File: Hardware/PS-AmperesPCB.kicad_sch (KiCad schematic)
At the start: 10 parts, among them J1 PeripheralCAN, J2 PeripheralCAN

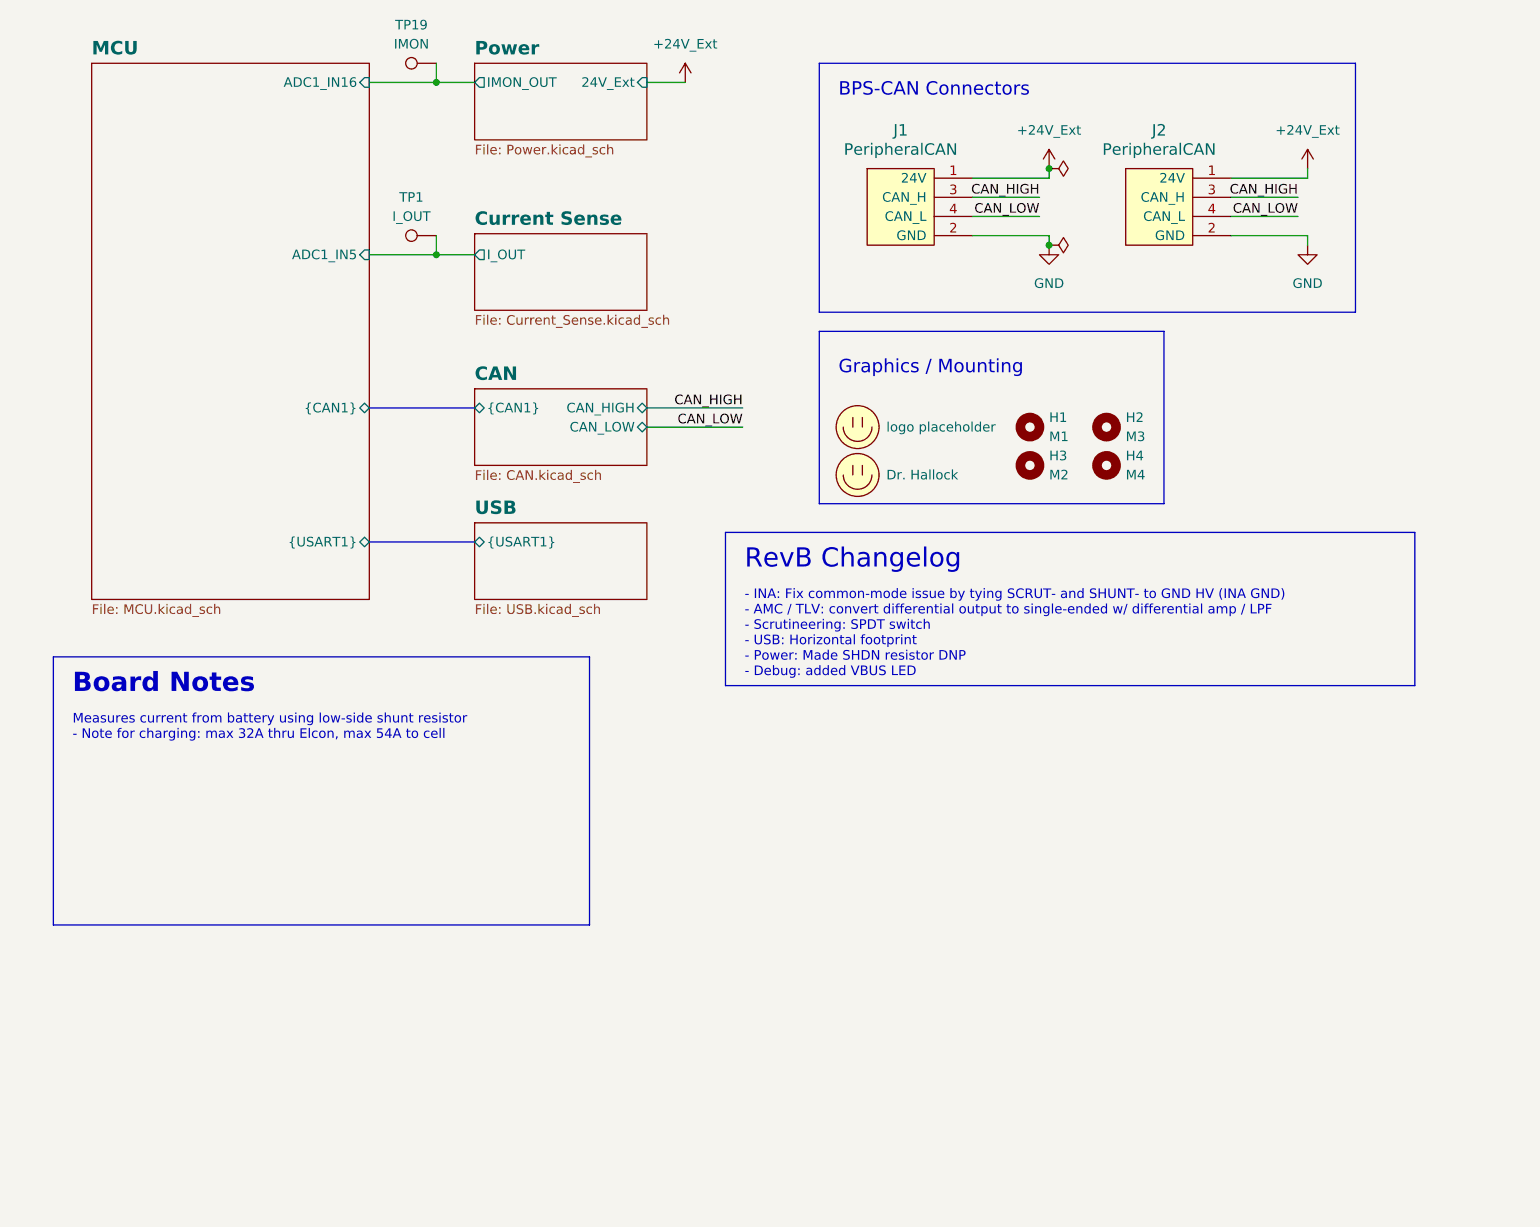
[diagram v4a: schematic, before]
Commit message: refactored and added LPF docs; added fuse, boot_gpio from USB-UART chip
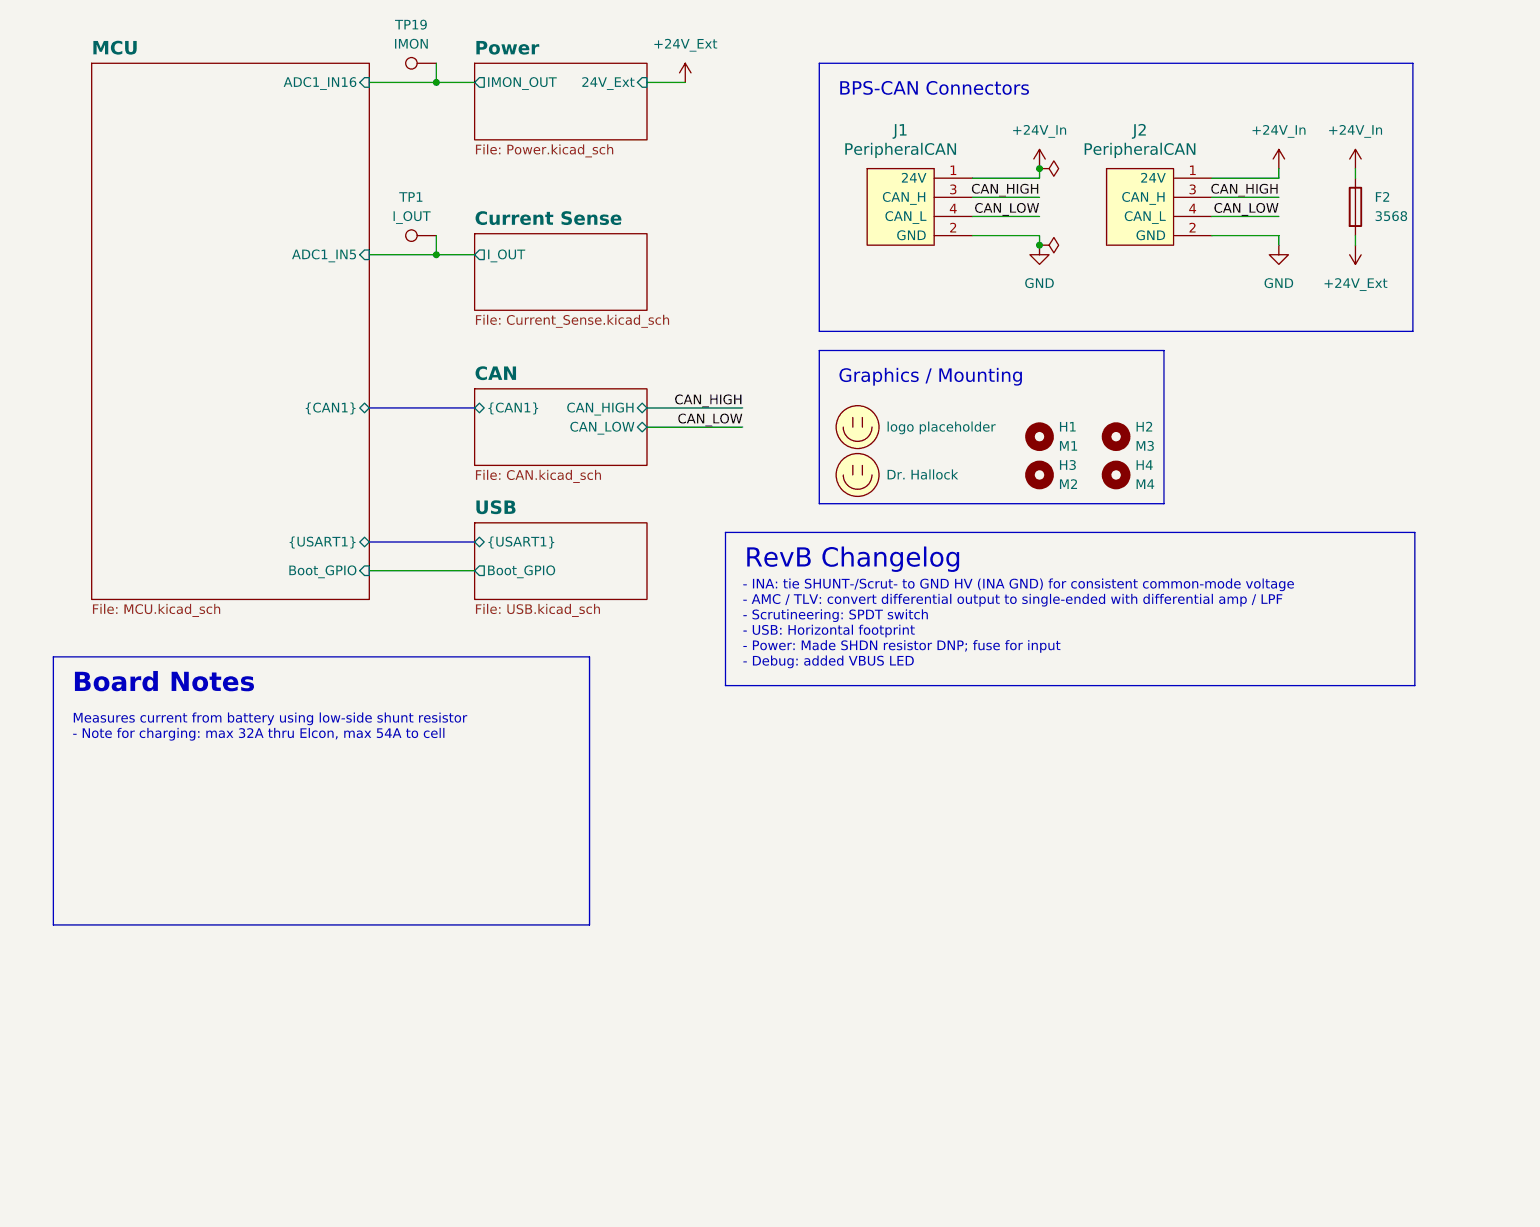
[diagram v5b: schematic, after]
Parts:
- added F2: 3568, Fuse:Fuseholder_Blade_Mini_Keystone_3568, symbol Device:Fuse
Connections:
- net +24V_Ext: now also F2.2; no longer J1.1 (24V), J2.1 (24V)
- new net +24V_In: F2.1, J1.1 (24V), J2.1 (24V)
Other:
- sheet MCU ports: added Boot_GPIO; removed none
- sheet USB ports: added Boot_GPIO; removed none
- note added: "- INA: tie SHUNT-/Scrut- to GND HV (INA GND) for consistent common-mode voltage - AMC / TLV: convert differential output to single-ended with differential amp / LPF - Scrutineering: SPDT switch - USB: Horizontal footprint - Power: Made SHDN resistor DNP; fuse for input - Debug: added VBUS LED"
- note removed: "- INA: Fix common-mode issue by tying SCRUT- and SHUNT- to GND HV (INA GND) - AMC / TLV: convert differential output to single-ended w/ differential amp / LPF - Scrutineering: SPDT switch - USB: Horizontal footprint - Power: Made SHDN resistor DNP - Debug: added VBUS LED"
- moved on the sheet: H1, H2, H3, H4, J2

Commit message: slightly cooked
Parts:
- TP19: footprint TestPoint:TestPoint_Keystone_5005-5009_Compact -> TestPoint:TestPoint_Pad_1.0x1.0mm
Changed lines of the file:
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@@
 			)
 		)
-		(property "Footprint" "TestPoint:TestPoint_Keystone_5005-5009_Compact"
+		(property "Footprint" "TestPoint:TestPoint_Pad_1.0x1.0mm"
 			(at 66.04 15.24 0)
 			(effects

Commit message: layout stuff
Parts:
- TP1: footprint TestPoint:TestPoint_Keystone_5005-5009_Compact -> Connector_PinHeader_2.54mm:PinHeader_1x01_P2.54mm_Vertical
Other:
- note added: "I_OUT = (current * shunt * gain) + Vref (V) = (current * 0.025) + 1.25 (V)"
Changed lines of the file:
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@@
 	(paper "A5")
 	(rectangle
-		(start 15.24 99.06)
+		(start 15.24 96.52)
 		(end 86.36 134.62)
 		(stroke
@@
 	(text "Board Notes"
 		(exclude_from_sim no)
-		(at 17.78 104.14 0)
+		(at 17.78 101.6 0)
 		(effects
 			(font
@@
 		)
 	)
+	(text "I_OUT = (current * shunt * gain) + Vref (V) \n	  = (current * 0.025) + 1.25 (V)"
+		(exclude_from_sim no)
+		(at 17.78 107.696 0)
+		(effects
+			(font
+				(size 1.27 1.27)
+				(thickness 0.254)
+				(bold yes)
+			)
+			(justify left top)
+		)
+	)
 	(text "Graphics / Mounting"
 		(exclude_from_sim no)
@@
 	(text "Measures current from battery using low-side shunt resistor\n- Note for charging: max 32A thru Elcon, max 54A to cell\n"
 		(exclude_from_sim no)
-		(at 17.78 106.68 0)
+		(at 17.78 102.616 0)
 		(effects
 			(font
@@
 			(table_cell "Measurable Current Range"
 				(exclude_from_sim no)
-				(at 17.78 122.936 0)
+				(at 17.78 123.444 0)
 				(size 27.94 3.048)
 				(margins 0.9525 0.9525 0.9525 0.9525)
@@
 			(table_cell "Current (A)"
 				(exclude_from_sim no)
-				(at 45.72 122.936 0)
+				(at 45.72 123.444 0)
 				(size 15.24 3.048)
 				(margins 0.9525 0.9525 0.9525 0.9525)
@@
 			(table_cell "I_OUT Reading (V)"
 				(exclude_from_sim no)
-				(at 60.96 122.936 0)
+				(at 60.96 123.444 0)
 				(size 20.32 3.048)
 				(margins 0.9525 0.9525 0.9525 0.9525)
@@
 			(table_cell "Max Charge (-)"
 				(exclude_from_sim no)
-				(at 17.78 125.984 0)
+				(at 17.78 126.492 0)
 				(size 27.94 3.048)
 				(margins 0.9525 0.9525 0.9525 0.9525)
@@
 			(table_cell "-46 A"
 				(exclude_from_sim no)
-				(at 45.72 125.984 0)
+				(at 45.72 126.492 0)
 				(size 15.24 3.048)
 				(margins 0.9525 0.9525 0.9525 0.9525)
@@
 			(table_cell "0.1 V"
 				(exclude_from_sim no)
-				(at 60.96 125.984 0)
+				(at 60.96 126.492 0)
 				(size 20.32 3.048)
 				(margins 0.9525 0.9525 0.9525 0.9525)
@@
 			(table_cell "Max Discharge (+)"
 				(exclude_from_sim no)
-				(at 17.78 129.032 0)
+				(at 17.78 129.54 0)
 				(size 27.94 3.048)
 				(margins 0.9525 0.9525 0.9525 0.9525)
@@
 			(table_cell "+78 A"
 				(exclude_from_sim no)
-				(at 45.72 129.032 0)
+				(at 45.72 129.54 0)
 				(size 15.24 3.048)
 				(margins 0.9525 0.9525 0.9525 0.9525)
@@
 			(table_cell "3.2 V"
 				(exclude_from_sim no)
-				(at 60.96 129.032 0)
+				(at 60.96 129.54 0)
 				(size 20.32 3.048)
 				(margins 0.9525 0.9525 0.9525 0.9525)
@@
 			(table_cell "Battery Current Range"
 				(exclude_from_sim no)
-				(at 17.78 111.76 0)
+				(at 17.78 112.268 0)
 				(size 27.94 3.048)
 				(margins 0.9525 0.9525 0.9525 0.9525)
@@
 			(table_cell "Current (A)"
 				(exclude_from_sim no)
-				(at 45.72 111.76 0)
+				(at 45.72 112.268 0)
 				(size 15.24 3.048)
 				(margins 0.9525 0.9525 0.9525 0.9525)
@@
 			(table_cell "I_OUT Reading (V)"
 				(exclude_from_sim no)
-				(at 60.96 111.76 0)
+				(at 60.96 112.268 0)
 				(size 20.32 3.048)
 				(margins 0.9525 0.9525 0.9525 0.9525)
@@
 			(table_cell "Max Charge (-)"
 				(exclude_from_sim no)
-				(at 17.78 114.808 0)
+				(at 17.78 115.316 0)
 				(size 27.94 3.048)
 				(margins 0.9525 0.9525 0.9525 0.9525)
@@
 			(table_cell "-32 A"
 				(exclude_from_sim no)
-				(at 45.72 114.808 0)
+				(at 45.72 115.316 0)
 				(size 15.24 3.048)
 				(margins 0.9525 0.9525 0.9525 0.9525)
@@
 			(table_cell "0.45 V"
 				(exclude_from_sim no)
-				(at 60.96 114.808 0)
+				(at 60.96 115.316 0)
 				(size 20.32 3.048)
 				(margins 0.9525 0.9525 0.9525 0.9525)
@@
 			(table_cell "Max Discharge (+)"
 				(exclude_from_sim no)
-				(at 17.78 117.856 0)
+				(at 17.78 118.364 0)
 				(size 27.94 3.048)
 				(margins 0.9525 0.9525 0.9525 0.9525)
@@
 			(table_cell "+70 A"
 				(exclude_from_sim no)
-				(at 45.72 117.856 0)
+				(at 45.72 118.364 0)
 				(size 15.24 3.048)
 				(margins 0.9525 0.9525 0.9525 0.9525)
@@
 			(table_cell "3.0 V"
 				(exclude_from_sim no)
-				(at 60.96 117.856 0)
+				(at 60.96 118.364 0)
 				(size 20.32 3.048)
 				(margins 0.9525 0.9525 0.9525 0.9525)
@@
 			)
 		)
-		(property "Footprint" "TestPoint:TestPoint_Keystone_5005-5009_Compact"
+		(property "Footprint" "Connector_PinHeader_2.54mm:PinHeader_1x01_P2.54mm_Vertical"
 			(at 66.04 38.1 0)
 			(effects

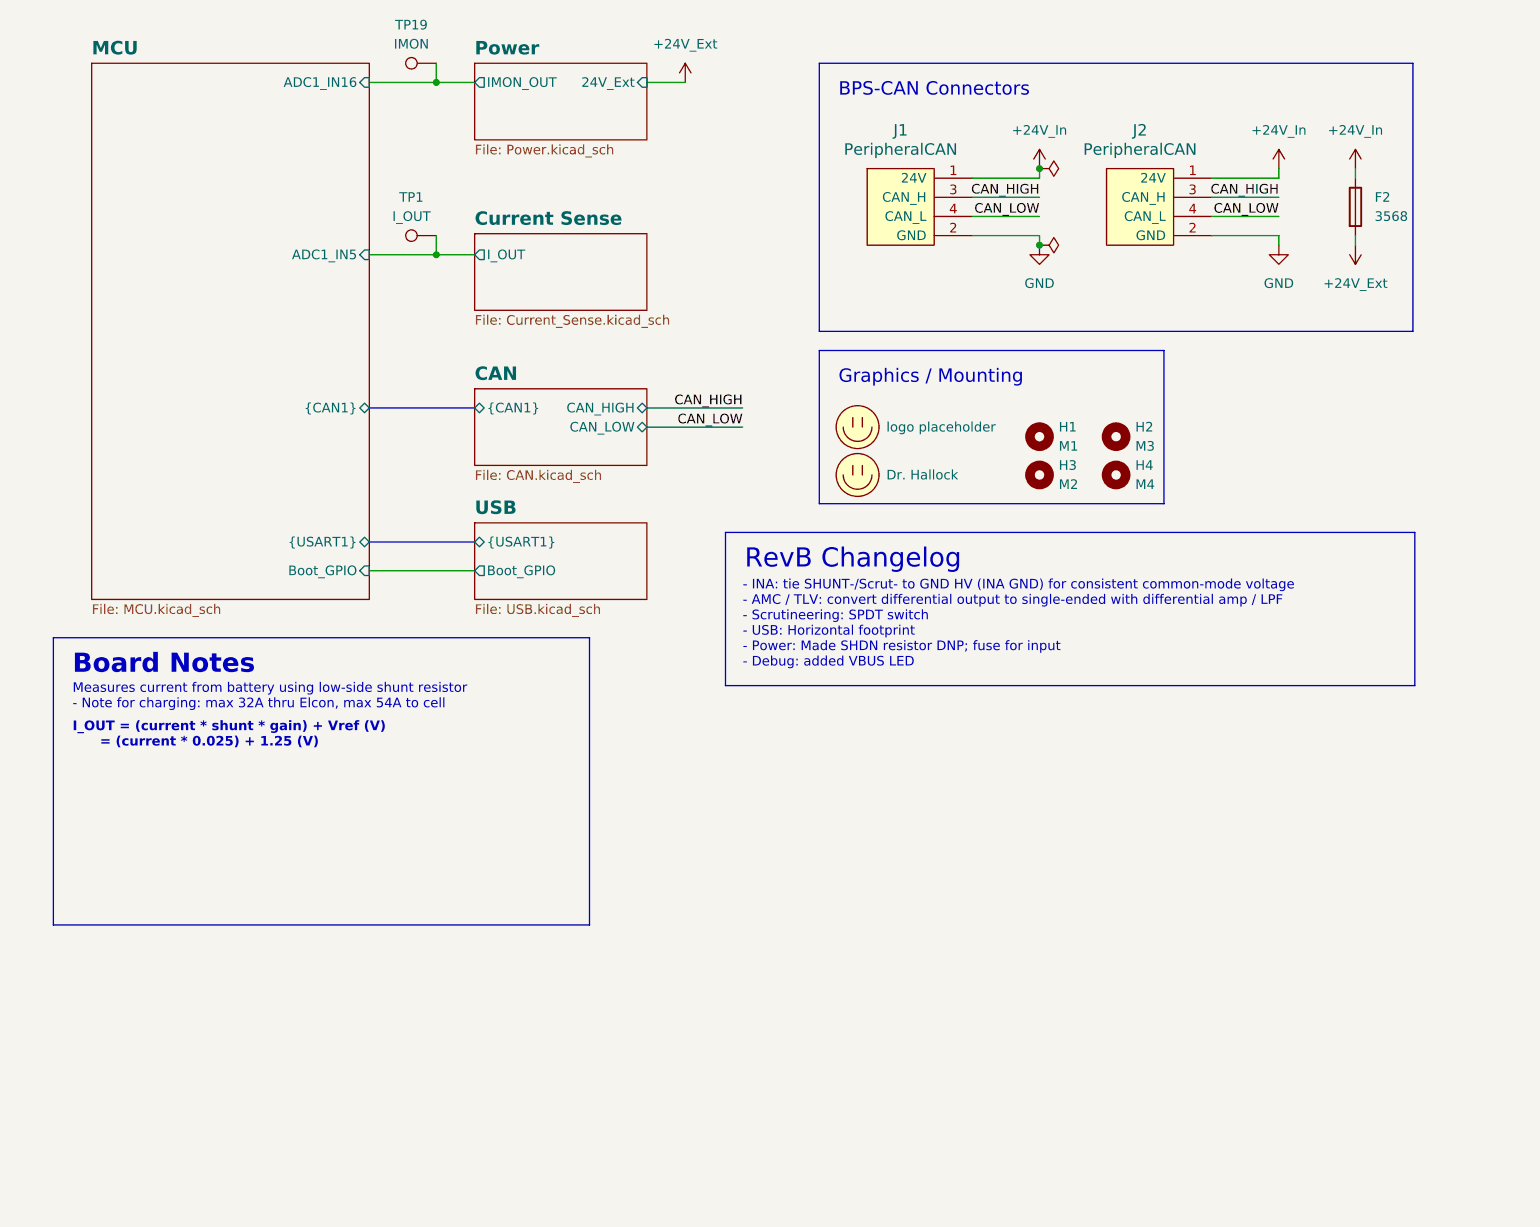
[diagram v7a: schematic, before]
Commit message: post review council sch changes: shielded connectors, removed SHDN resistor, diode OR for boot, standardized resistors
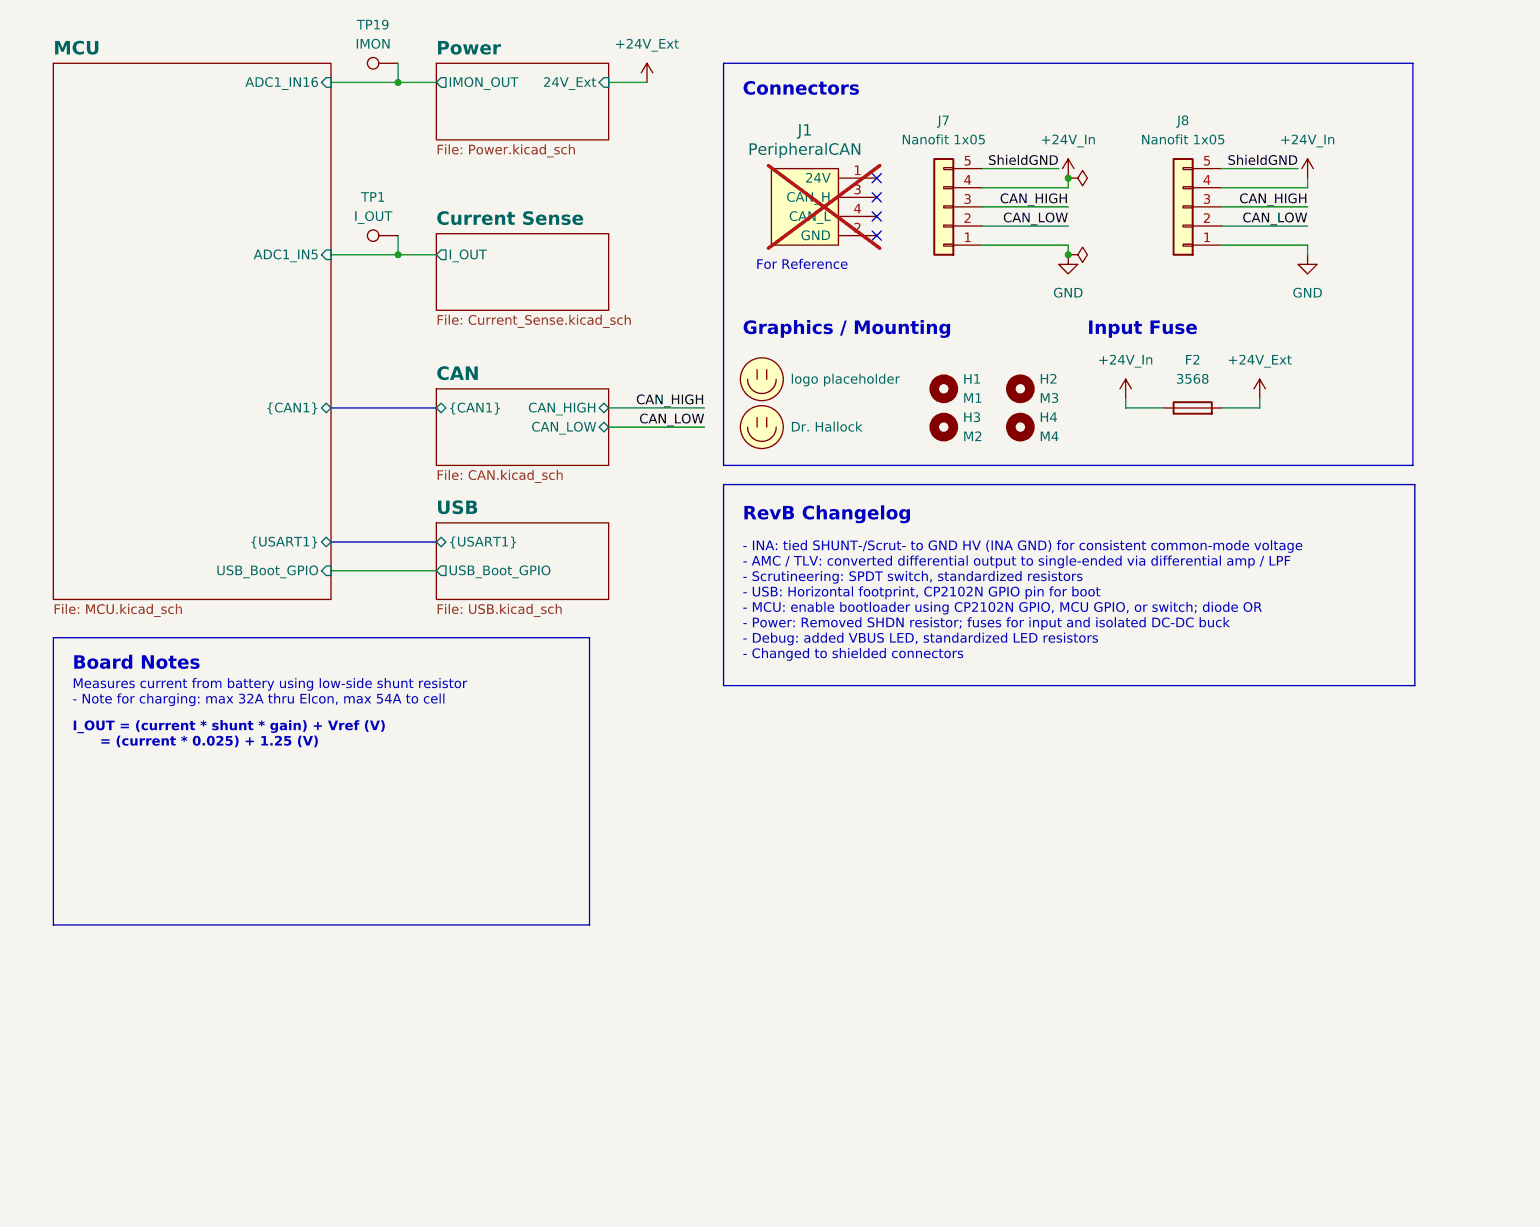
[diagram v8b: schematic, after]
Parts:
- removed J2: PeripheralCAN, UTSVT_Connectors:Molex_Nano-Fit_105309-xx04_1x04_P2.50mm_Vertical, symbol utsvt-connectors:PeripheralCANConnector
- added J7, J8: Nanofit 1x05, symbol Connector_Generic:Conn_01x05
- J1: now not fitted; now left out of the parts list
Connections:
- net +24V_In: now also J7.4 (Pin_4), J8.4 (Pin_4); no longer J1.1 (24V)
- net CAN_HIGH: now also J7.3 (Pin_3), J8.3 (Pin_3); no longer J1.3 (CAN_H)
- net CAN_LOW: now also J7.2 (Pin_2), J8.2 (Pin_2); no longer J1.4 (CAN_L)
- net GND: now also J7.1 (Pin_1), J8.1 (Pin_1); no longer J1.2 (GND)
- new net ShieldGND: J7.5 (Pin_5), J8.5 (Pin_5)
- no-connect marks 0 -> 4
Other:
- sheet MCU ports: added USB_Boot_GPIO; removed Boot_GPIO
- sheet USB ports: added USB_Boot_GPIO; removed Boot_GPIO
- note added: "- INA: tied SHUNT-/Scrut- to GND HV (INA GND) for consistent common-mode voltage - AMC / TLV: converted differential output to single-ended via differential amp / LPF - Scrutineering: SPDT switch, standardized resistors - USB: Horizontal footprint, CP2102N GPIO pin for boot - MCU: enable bootloader using CP2102N GPIO, MCU GPIO, or switch; diode OR - Power: Removed SHDN resistor; fuses for input a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"
- note added: "Connectors"
- note added: "For Reference"
- note added: "Input Fuse"
- note removed: "- INA: tie SHUNT-/Scrut- to GND HV (INA GND) for consistent common-mode voltage - AMC / TLV: convert differential output to single-ended with differential amp / LPF - Scrutineering: SPDT switch - USB: Horizontal footprint - Power: Made SHDN resistor DNP; fuse for input - Debug: added VBUS LED"
- note removed: "BPS-CAN Connectors"
- moved on the sheet: F2, H1, H2, H3, H4, TP1, TP19
